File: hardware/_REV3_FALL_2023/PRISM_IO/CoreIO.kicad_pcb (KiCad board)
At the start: 2 copper layers, 61 x 88.9 mm, 44 parts, among them J1 Conn_01x04_Socket, J2 COTS_SWITCH_PLUG, J3 PYRO 1, J4 PYRO 2, Q1 AO3400A, Q2 AO3400A, U1 TMC2209_SILENTSTEPSTICK, U2 LD1117S12TR_SOT223

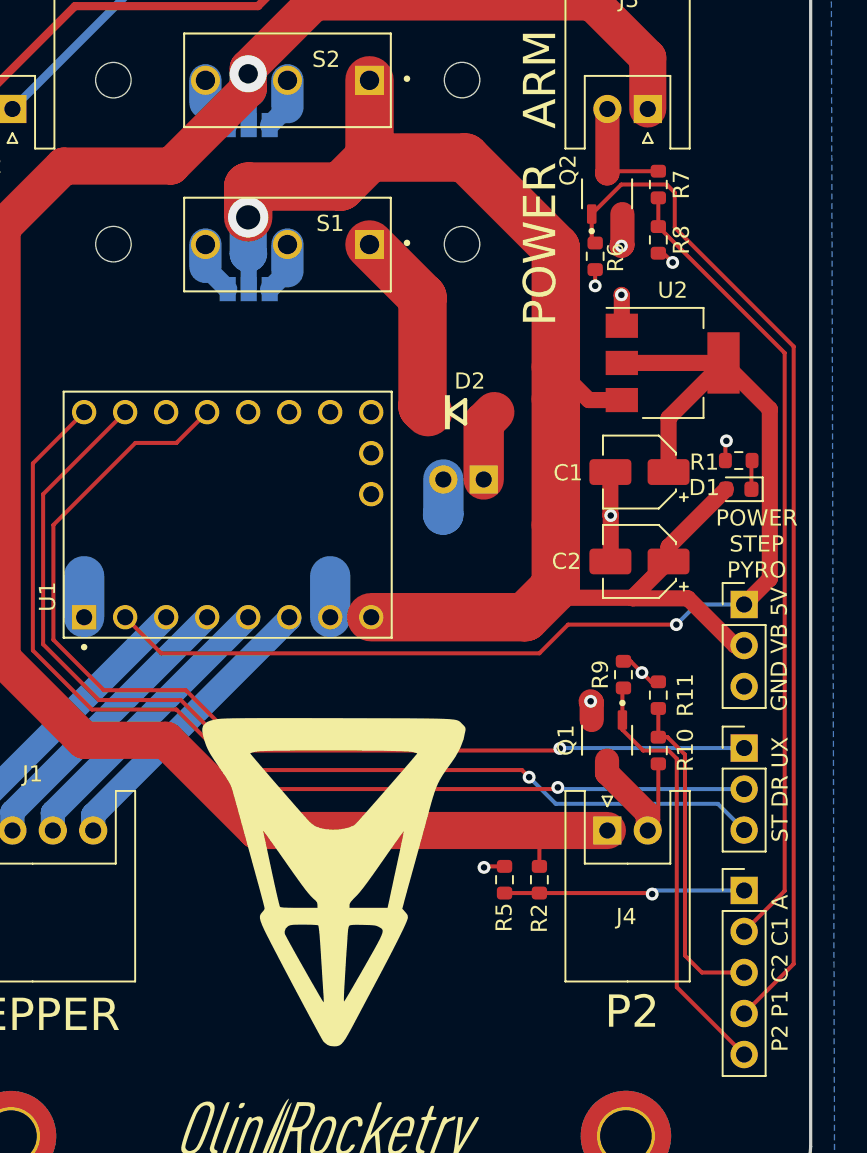
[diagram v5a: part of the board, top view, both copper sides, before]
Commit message: add resistors to IO
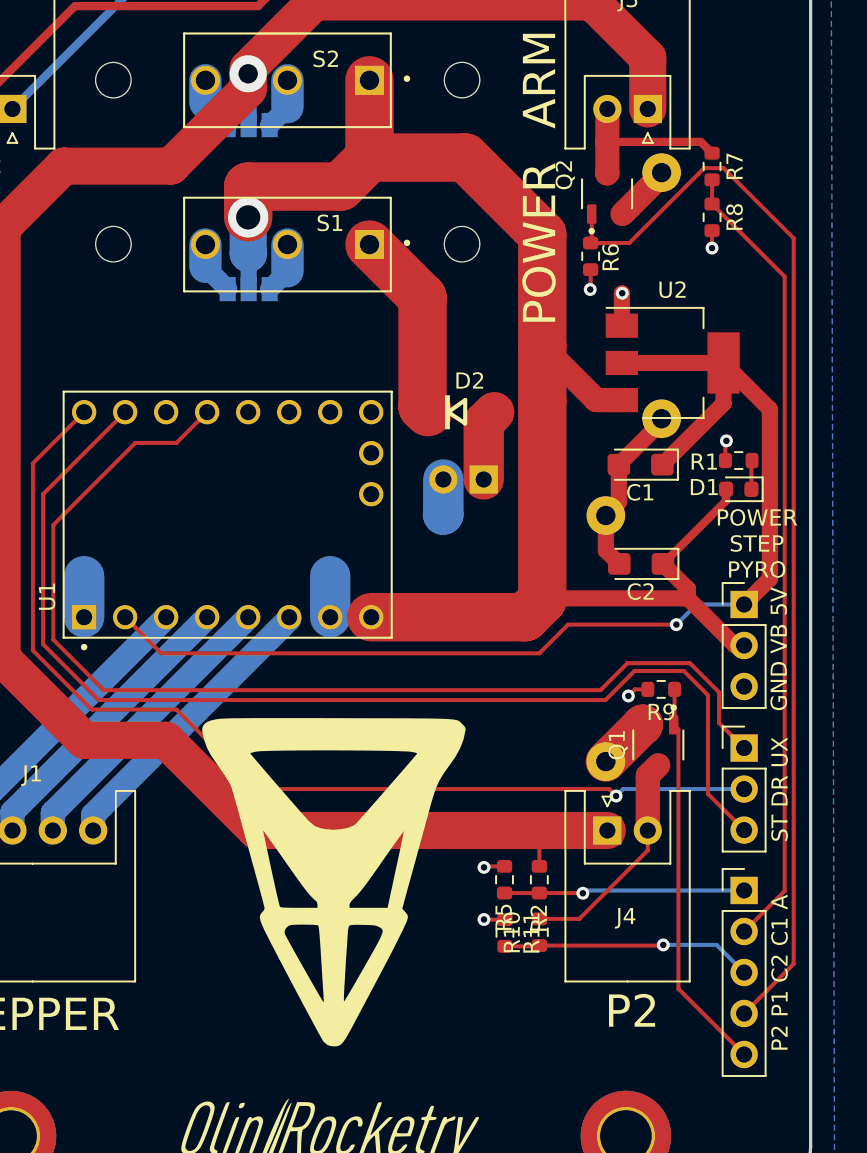
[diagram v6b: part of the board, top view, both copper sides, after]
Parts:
- added R3: 6.8, Resistor_THT:R_Axial_DIN0414_L11.9mm_D4.5mm_P15.24mm_Horizontal, B.Cu at (169.1, 76.6)
- added R4: 6.8, Resistor_THT:R_Axial_DIN0414_L11.9mm_D4.5mm_P15.24mm_Horizontal, B.Cu at (165.7, 113.1)
- C1, C2: footprint Capacitor_SMD:CP_Elec_4x5.4 -> Capacitor_Tantalum_SMD:CP_EIA-3216-18_Kemet-A
- Q2: footprint rocketry_footprints:SOT95P280X125-3N -> AO3400A.pretty-master:SOT95P280X125-3N
- moved R11 17.5 mm to (159.4, 123.7)
- moved R10 13.4 mm to (161.5, 123.6), turned to -90 degrees
- moved R8 3.61 mm to (172.2, 79.4)
- moved R7 3.51 mm to (172.2, 76.2)
- moved Q1 3.19 mm to (168.9, 112.0)
- moved R9 2.51 mm to (169.1, 108.6), turned to 180 degrees
- moved C1 0.46 mm to (167.8, 94.7)
- moved R6 0.28 mm to (164.7, 81.8)
- moved C2 0.18 mm to (167.8, 100.8)
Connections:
- Q1 pad 2: GND -> Net-(Q1-Pad2)
- Q2 pad 2: GND -> Net-(Q2-Pad2)
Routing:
- net /STEP: track 64.7 -> 69.7 mm, vias 1 -> 0
- net /CONT 2: track 20.4 -> 15.6 mm, vias 0 -> 1
- net /PYRO 1: track 63.1 -> 67.4 mm
- net Net-(J4-Pin_2): track 9.78 -> 14.0 mm
- net Net-(J3-Pin_2): track 7.24 -> 11.0 mm
- net Net-(Q2-Pad2): track 0.00 -> 3.57 mm
- net Net-(Q1-Pad2): track 0.00 -> 3.25 mm
- net /V_BATT: track 93.8 -> 96.4 mm
- net /UART: track 65.2 -> 67.6 mm, vias 1 -> 0
- net GND: track 25.3 -> 27.6 mm, vias 9 -> 7
- net /PYRO 2: track 26.8 -> 24.5 mm

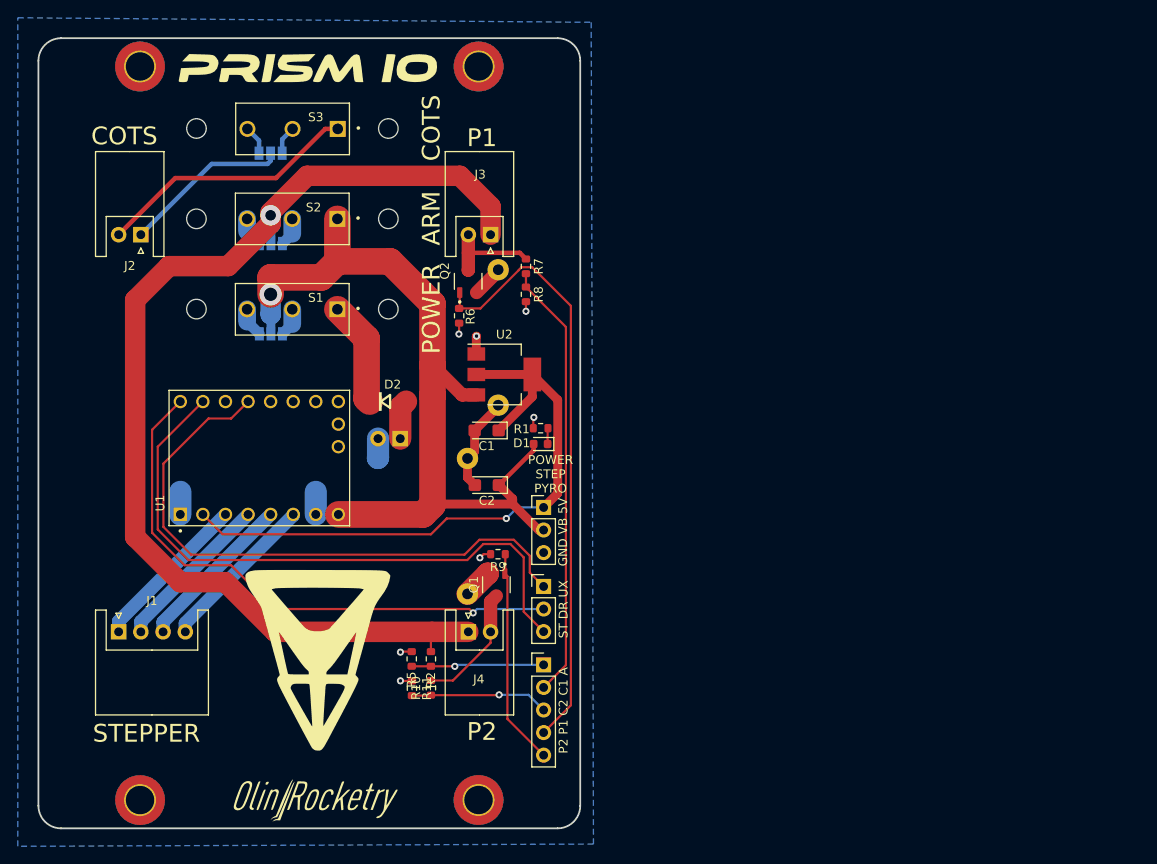
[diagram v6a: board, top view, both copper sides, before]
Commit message: Fixed Silkscreen and removed power plane
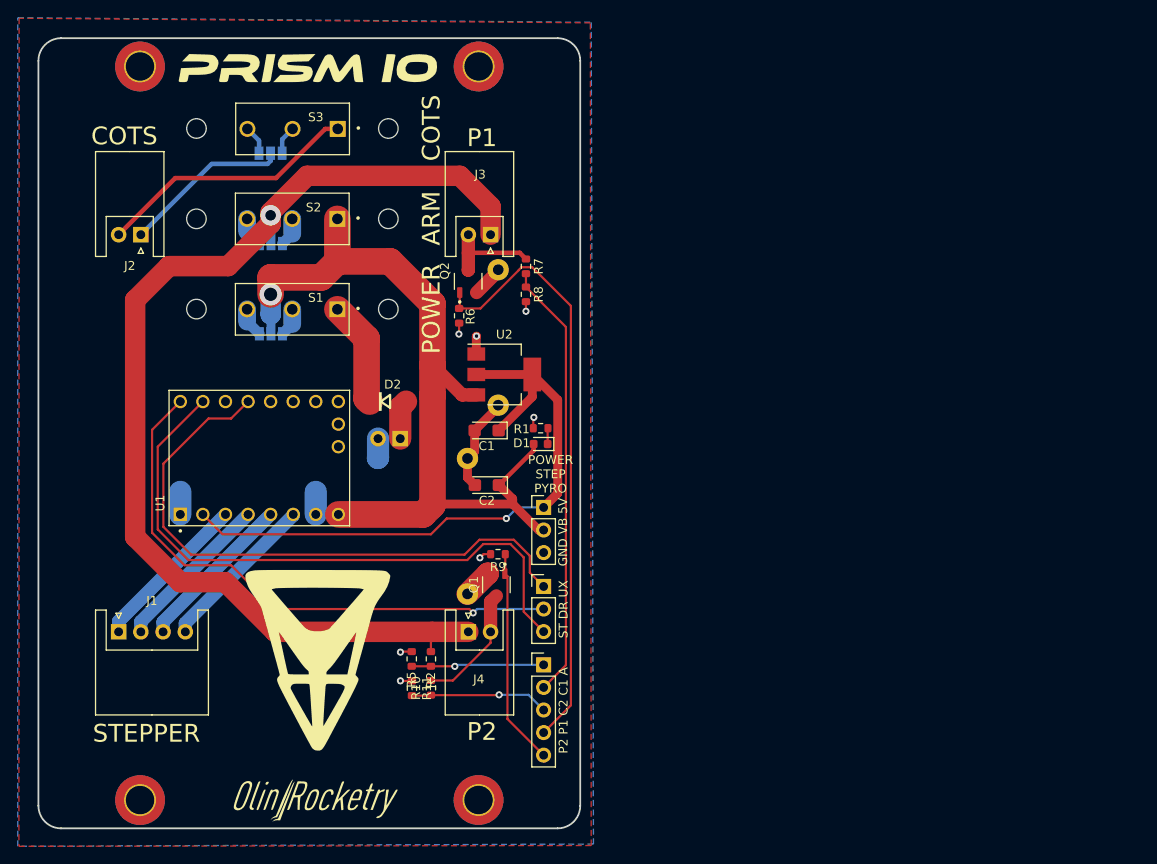
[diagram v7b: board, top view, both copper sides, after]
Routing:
- added copper zone on F.Cu, net GND

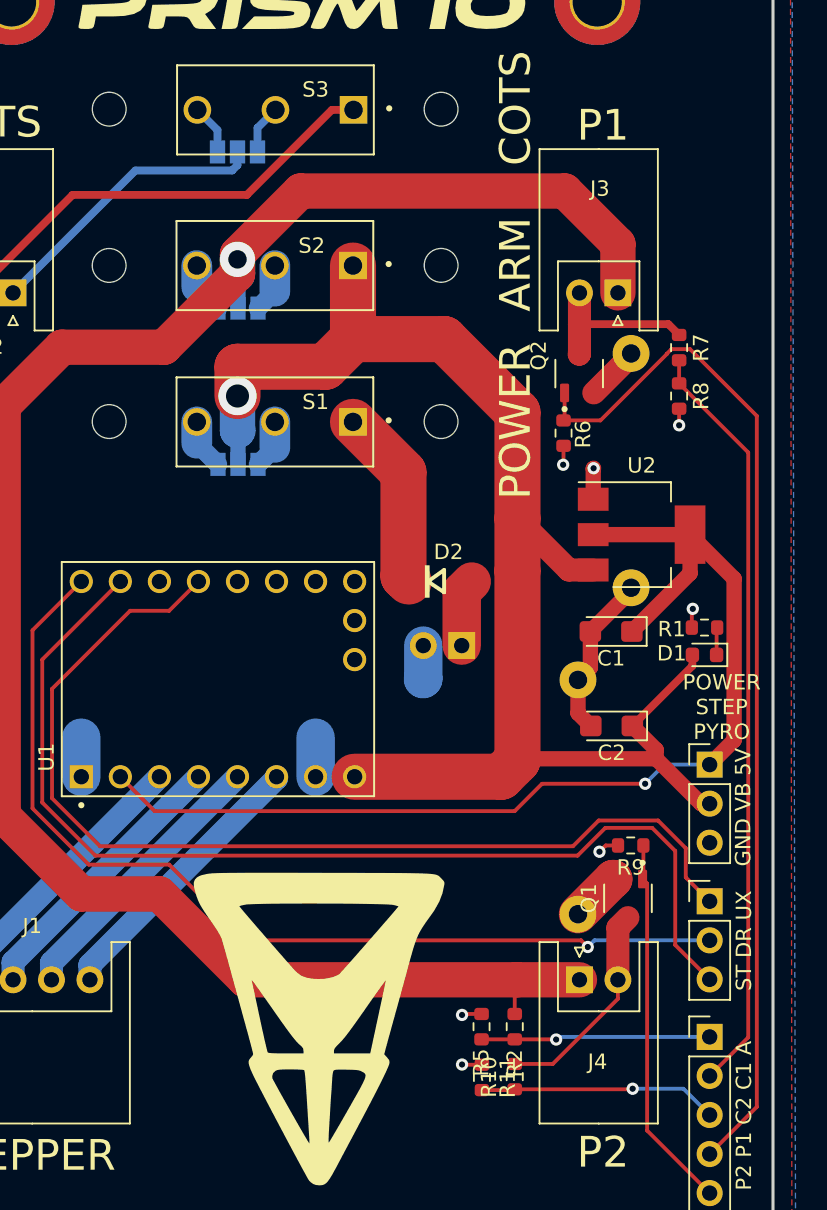
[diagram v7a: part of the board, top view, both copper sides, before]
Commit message: Updated Core IO connectors to match updated Teensy board and change stepper to 3.3V
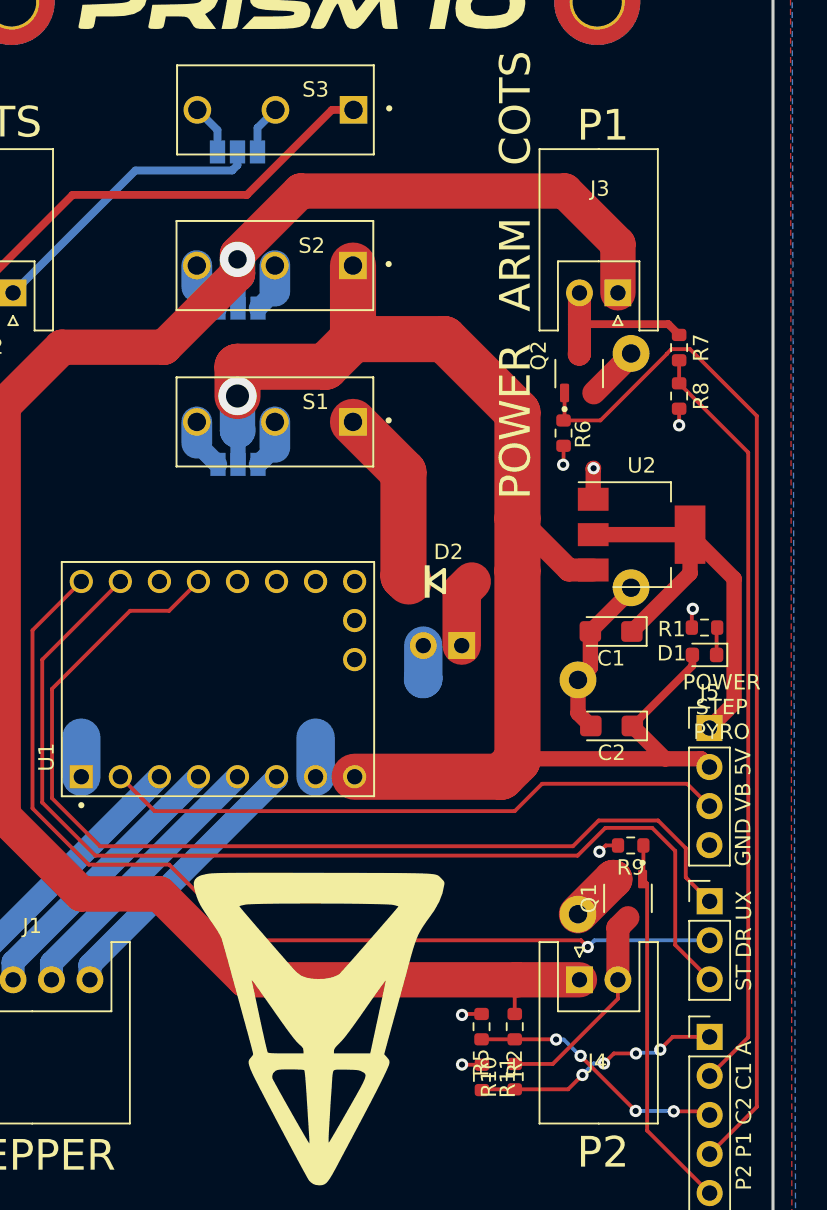
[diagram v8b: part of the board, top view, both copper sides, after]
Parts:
- removed the ? at (135.2, 70.9)
- removed Power2: Conn_01x03_Socket, Connector_PinHeader_2.54mm:PinHeader_1x03_P2.54mm_Vertical
- removed REF** (x5): MountingHole_2.2mm_M2, MountingHole:MountingHole_2.2mm_M2
- added J5: Conn_01x04_Socket, Connector_PinHeader_2.54mm:PinHeader_1x04_P2.54mm_Vertical, F.Cu at (174.2, 101.0)
- Q2: footprint AO3400A.pretty-master:SOT95P280X125-3N -> rocketry_footprints:SOT95P280X125-3N
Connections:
- Pyro2 pad 1: /ARM -> /CONT 2
- Pyro2 pad 3: /CONT 2 -> /ARM
- U1 pad 2: /5V -> /3.3V
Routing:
- net /5V: track 72.5 -> 28.6 mm, vias 1 -> 0
- net /3.3V: track 0.00 -> 40.6 mm
- net /ARM: track 14.9 -> 17.5 mm, vias 1 -> 4
- net /V_BATT: track 96.4 -> 95.3 mm
- net /CONT 2: track 15.6 -> 16.6 mm, vias 1 -> 4
